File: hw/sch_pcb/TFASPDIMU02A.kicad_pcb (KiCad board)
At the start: 2 copper layers, 30 x 15 mm, 39 parts, among them J1 SM04B-GHS-TB, M1 HOLE_TF, M2 HOLE_TF, M3 HOLE_TF, M4 HOLE_TF, M7 HOLE_TF, M8 HOLE_TF, U1 SDP3x, U2 ICM-20948, U3 TCA9617A, U4 MIC5504-3.3YM5-TR, U5 MIC5504-1.8YM5-TR, U6 TCA9617A

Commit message: Edit PCB
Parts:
- added JP2: SolderJumper_3_Bridged12, Jumper:SolderJumper-3_P1.3mm_Bridged12_RoundedPad1.0x1.5mm, F.Cu at (4.32, -3.05)
- JP1: moved to F.Cu
- moved JP1 8.76 mm to (17.3, -12.2), turned to 90 degrees
- moved R3 4.35 mm to (18.0, -10.0), turned to 0 degrees
- moved C8 3.91 mm to (16.3, -13.1), turned to -90 degrees
- moved M4 2.97 mm to (22.0, 2.92)
- moved U5 1.77 mm to (18.9, -12.8)
- moved C6 1.47 mm to (22.9, -12.6), turned to 0 degrees
- moved C4 1.47 mm to (14.6, -12.4)
- moved C9 1.45 mm to (15.7, -5.59), turned to -90 degrees
- moved R11 1.33 mm to (21.1, -10.0), turned to 180 degrees
- moved C5 1.03 mm to (25.5, -1.65), turned to 0 degrees
- moved U2 1.02 mm to (13.2, -9.53)
- moved C2 0.80 mm to (11.8, -12.3), turned to 180 degrees
- moved C12 0.76 mm to (18.5, -4.57), turned to 90 degrees
- moved D2 0.74 mm to (25.5, -13.2)
- moved C11 0.62 mm to (22.9, -11.2), turned to 0 degrees
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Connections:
- R10 pad 1: Net-(U1-Pad9) -> Net-(R10-Pad1)
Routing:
- net +1V8: track 0.00 -> 40.7 mm, vias 0 -> 2
- net +3V3: track 5.36 -> 42.7 mm, vias 0 -> 5
- net +5V: track 0.00 -> 32.8 mm
- net /P_SCL_1V8: track 0.00 -> 12.7 mm, vias 0 -> 2
- net /SCL_3V3: track 0.00 -> 11.9 mm, vias 0 -> 2
- net /P_SDA_1V8: track 0.00 -> 8.94 mm, vias 0 -> 2
- net /SDA_3V3: track 0.00 -> 8.74 mm, vias 0 -> 2
- net /SCL_1V8: track 0.00 -> 8.69 mm, vias 0 -> 2
- net /SDA_1V8: track 0.00 -> 8.11 mm, vias 0 -> 2
- net Net-(U1-Pad9): track 0.73 -> 7.92 mm, vias 0 -> 1
- net Net-(JP1-Pad2): track 0.00 -> 5.67 mm, vias 0 -> 1
- net GND: track 0.00 -> 4.65 mm, vias 0 -> 46
- net Net-(R1-Pad1): track 0.00 -> 4.65 mm
- net Net-(R11-Pad1): track 0.00 -> 3.40 mm
- net Net-(C4-Pad1): track 0.00 -> 1.72 mm
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
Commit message: Dimensions and layout improvement.
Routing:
- net +1V8: track 40.7 -> 42.1 mm
- net Net-(R1-Pad1): track 4.65 -> 3.85 mm
- net GND: track 4.65 -> 5.20 mm, vias 46 -> 47

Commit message: Edit PCB
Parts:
- moved U1 0.10 mm to (5.40, -8.15)
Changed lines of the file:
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@@
-(kicad_pcb (version 20210722) (generator pcbnew)
+(kicad_pcb (version 20210228) (generator pcbnew)
   (general
     (thickness 1.6)
@@
       (effects (font (size 1 1) (thickness 0.15)))
     )
-    (fp_poly (pts
-        (xy -0.9 -0.3)
-        (xy -0.4 -0.3)
-        (xy -0.4 0.3)
-        (xy -0.9 0.3)
-      ) (layer "F.Cu") (width 0) (fill solid))
+    (fp_poly (pts (xy -0.9 -0.3)
+      (xy -0.4 -0.3)
+      (xy -0.4 0.3)
+      (xy -0.9 0.3)) (layer "F.Cu") (width 0) (fill solid))
     (fp_line (start 1.4 1) (end -1.4 1) (layer "F.SilkS") (width 0.12))
     (fp_line (start -1.2 1.2) (end -1.5 1.5) (layer "F.SilkS") (width 0.12))
@@
         (gr_circle (center 0 -0.25) (end 0.5 -0.25) (width 0) (fill yes))
         (gr_poly (pts
-            (xy 0.55 0.75)
-            (xy 0 0.75)
-            (xy 0 -0.75)
-            (xy 0.55 -0.75)
-          ) (width 0) (fill yes))
+          (xy 0.55 0.75)
+          (xy 0 0.75)
+          (xy 0 -0.75)
+          (xy 0.55 -0.75)
+        ) (width 0) (fill yes))
       ))
     (pad "2" smd rect locked (at 0 0 180) (size 1 1.5) (layers "F.Cu" "F.Mask")
@@
         (gr_circle (center 0 -0.25) (end 0.5 -0.25) (width 0) (fill yes))
         (gr_poly (pts
-            (xy 0 0.75)
-            (xy -0.55 0.75)
-            (xy -0.55 -0.75)
-            (xy 0 -0.75)
-          ) (width 0) (fill yes))
+          (xy 0 0.75)
+          (xy -0.55 0.75)
+          (xy -0.55 -0.75)
+          (xy 0 -0.75)
+        ) (width 0) (fill yes))
       ))
   )
@@
       (effects (font (size 1 1) (thickness 0.15)))
     )
-    (fp_poly (pts
-        (xy -0.9 -0.3)
-        (xy -0.4 -0.3)
-        (xy -0.4 0.3)
-        (xy -0.9 0.3)
-      ) (layer "F.Cu") (width 0) (fill solid))
+    (fp_poly (pts (xy -0.9 -0.3)
+      (xy -0.4 -0.3)
+      (xy -0.4 0.3)
+      (xy -0.9 0.3)) (layer "F.Cu") (width 0) (fill solid))
     (fp_line (start -2.05 0.3) (end -2.05 -0.3) (layer "F.SilkS") (width 0.12))
     (fp_line (start -1.2 1.2) (end -0.9 1.5) (layer "F.SilkS") (width 0.12))
@@
         (gr_circle (center 0 -0.25) (end 0.5 -0.25) (width 0) (fill yes))
         (gr_poly (pts
-            (xy 0.55 0.75)
-            (xy 0 0.75)
-            (xy 0 -0.75)
-            (xy 0.55 -0.75)
-          ) (width 0) (fill yes))
+          (xy 0.55 0.75)
+          (xy 0 0.75)
+          (xy 0 -0.75)
+          (xy 0.55 -0.75)
+        ) (width 0) (fill yes))
       ))
     (pad "2" smd rect locked (at 0 0 90) (size 1 1.5) (layers "F.Cu" "F.Mask")
@@
         (gr_circle (center 0 -0.25) (end 0.5 -0.25) (width 0) (fill yes))
         (gr_poly (pts
-            (xy 0 0.75)
-            (xy -0.55 0.75)
-            (xy -0.55 -0.75)
-            (xy 0 -0.75)
-          ) (width 0) (fill yes))
+          (xy 0 0.75)
+          (xy -0.55 0.75)
+          (xy -0.55 -0.75)
+          (xy 0 -0.75)
+        ) (width 0) (fill yes))
       ))
   )
@@
   )
   (footprint "Mlab_IO:SDP3x" locked (layer "B.Cu")
-    (at 5.4 -8.25 180)
+    (at 5.4 -8.15 180)
     (property "Sheetfile" "TFASPDIMU02A.kicad_sch")
     (property "Sheetname" "")
@@
   (segment (start 5.888 -2.288) (end 5.334 -2.288) (width 0.3) (layer "B.Cu") (net 3))
   (segment (start 8.6085 -4.531) (end 8.509 -4.6305) (width 0.3) (layer "B.Cu") (net 3))
-  (segment (start 9.915 -5.442) (end 10.569 -6.096) (width 0.3) (layer "B.Cu") (net 3))
   (segment (start 21.717 -5.209) (end 22.957 -5.209) (width 0.4) (layer "B.Cu") (net 3))
   (segment (start 21.717 -5.209) (end 21.032081 -5.209) (width 0.4) (layer "B.Cu") (net 3))
@@
   (segment (start 5.334 -2.288) (end 5.212 -2.288) (width 0.3) (layer "B.Cu") (net 3))
   (segment (start 4.473 -3.429) (end 4.473 -3.027) (width 0.3) (layer "B.Cu") (net 3))
+  (segment (start 9.915 -4.531) (end 10.119 -4.531) (width 0.3) (layer "B.Cu") (net 3))
   (segment (start 15.51 -10.525) (end 16.129 -9.906) (width 0.2) (layer "B.Cu") (net 3))
+  (segment (start 10.119 -4.531) (end 10.569 -4.981) (width 0.3) (layer "B.Cu") (net 3))
   (segment (start 6.731 -2.536) (end 6.136 -2.536) (width 0.3) (layer "B.Cu") (net 3))
   (segment (start 21.032081 -5.209) (end 20.88797 -5.064889) (width 0.4) (layer "B.Cu") (net 3))
   (segment (start 22.851 -6.518) (end 22.851 -5.315) (width 0.3) (layer "B.Cu") (net 3))
   (segment (start 22.957 -5.209) (end 22.987 -5.179) (width 0.4) (layer "B.Cu") (net 3))
+  (segment (start 10.569 -4.981) (end 10.569 -6.096) (width 0.3) (layer "B.Cu") (net 3))
   (segment (start 6.136 -2.536) (end 5.888 -2.288) (width 0.3) (layer "B.Cu") (net 3))
   (segment (start 18.542 -2.766) (end 19.022 -2.766) (width 0.4) (layer "B.Cu") (net 3))
   (segment (start 16.129 -9.906) (end 17.397 -9.906) (width 0.2) (layer "B.Cu") (net 3))
-  (segment (start 9.915 -4.531) (end 9.915 -5.442) (width 0.3) (layer "B.Cu") (net 3))
   (segment (start 16.76409 -9.906) (end 16.868069 -9.802021) (width 0.2) (layer "B.Cu") (net 3))
   (segment (start 4.4 -5.55) (end 4.4 -3.502) (width 0.3) (layer "B.Cu") (net 3))
@@
       )
     )
+  )
+  (zone (net 0) (net_name "") (layers F&B.Cu) (hatch edge 0.508)
+    (connect_pads (clearance 0))
+    (min_thickness 0.254)
+    (keepout (tracks not_allowed) (vias not_allowed) (pads not_allowed ) (copperpour allowed) (footprints allowed))
+    (fill (thermal_gap 0.508) (thermal_bridge_width 0.508))
+    (polygon
+      (pts
+        (xy 14.224 -8.509)
+        (xy 12.192 -8.509)
+        (xy 12.192 -10.541)
+        (xy 14.224 -10.541)
+      )
+    )
+  )
+  (zone (net 0) (net_name "") (layers F&B.Cu) (hatch edge 0.508)
+    (connect_pads (clearance 0))
+    (min_thickness 0.254)
+    (keepout (tracks not_allowed) (vias not_allowed) (pads not_allowed ) (copperpour allowed) (footprints allowed))
+    (fill (thermal_gap 0.508) (thermal_bridge_width 0.508))
+    (polygon
+      (pts
+        (xy 14.224 -8.509)
+        (xy 12.192 -8.509)
+        (xy 12.192 -10.541)
+        (xy 14.224 -10.541)
+      )
+    )

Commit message: Edit PCB. #1
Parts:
- removed M4, M8: HOLE_TF, Mlab_Mechanical:dira_3mm
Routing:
- net Net-(JP2-Pad2): track 7.92 -> 6.59 mm

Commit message: Edit PCB
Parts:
- added G***: LOGO, MLAB_LOGA:TF 14x6,6, F.Cu at (8.38, -9.40)
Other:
- board text added: "TFASPDIMU02A"
- board text removed: "I2C 1 - 5V 2 - SCL 4 - SDA 7 - GND"

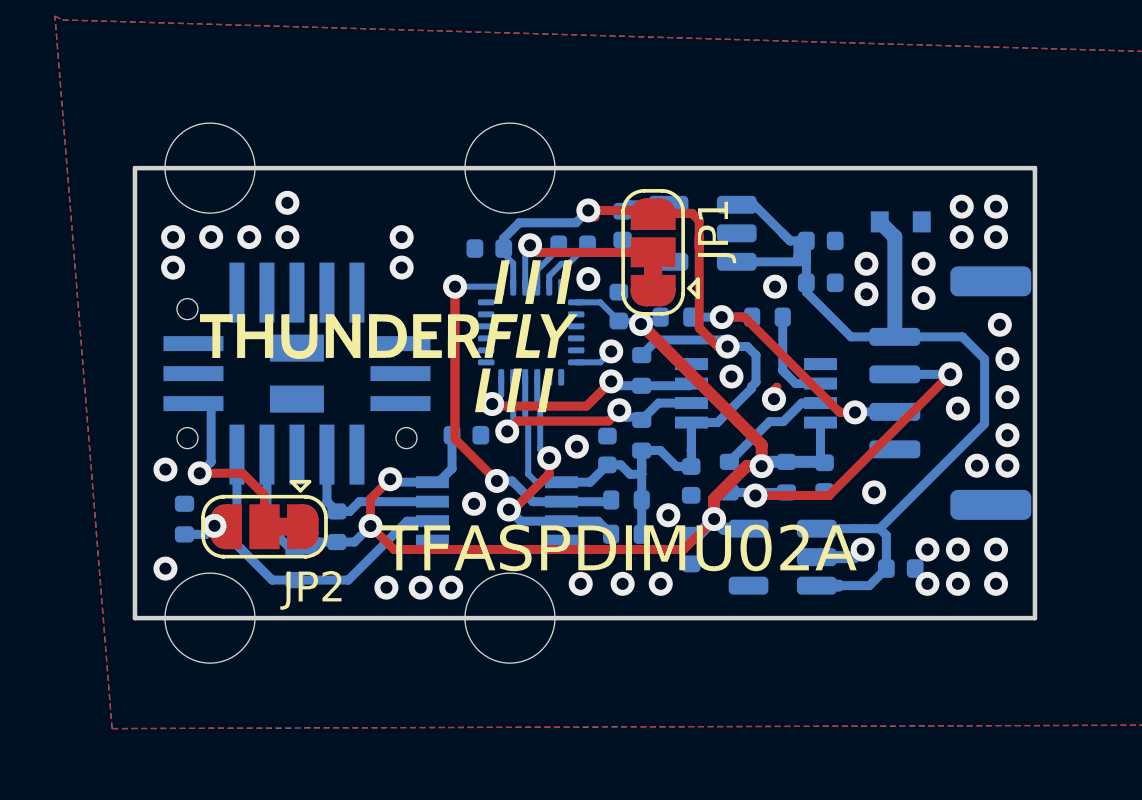
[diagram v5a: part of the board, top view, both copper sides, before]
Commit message: Layout and silkscreen improvements.
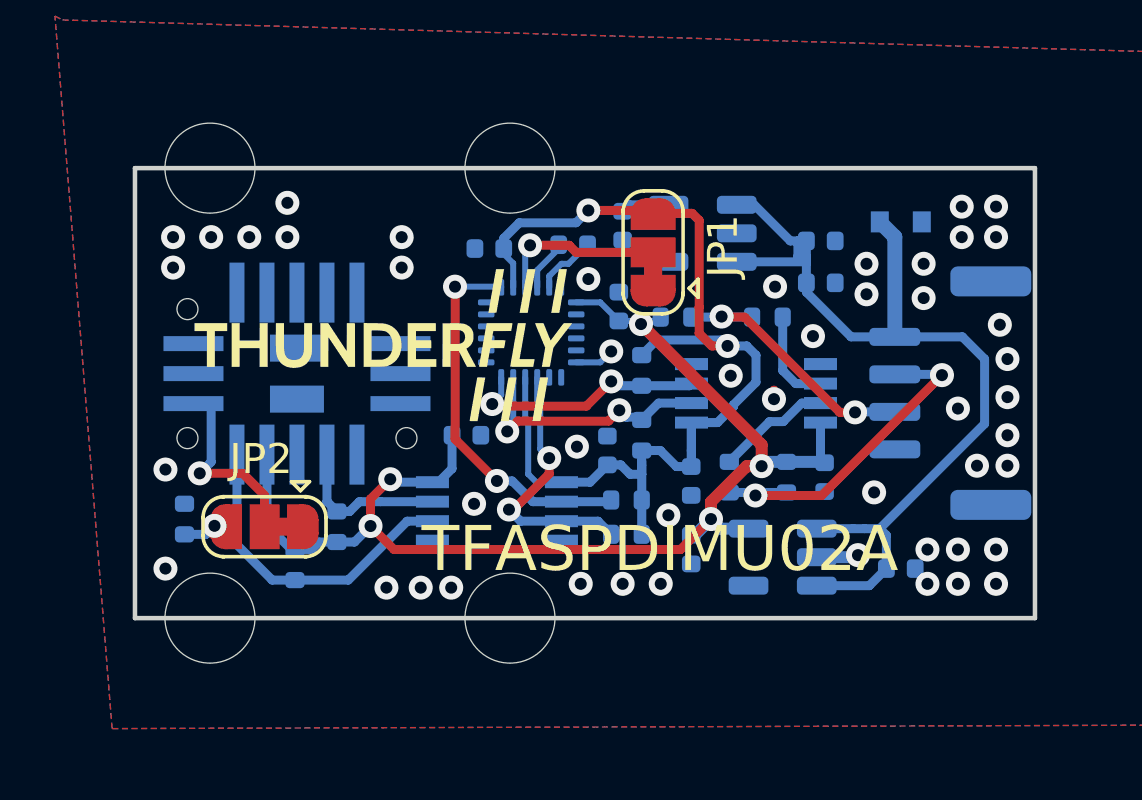
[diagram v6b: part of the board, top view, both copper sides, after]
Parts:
- moved G*** 0.35 mm to (8.20, -9.10)
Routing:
- net +1V8: track 42.1 -> 40.5 mm
- net +5V: track 32.8 -> 31.7 mm
- net /SCL_3V3: track 12.0 -> 11.5 mm
- net GND: track 5.20 -> 5.05 mm, vias 47 -> 48

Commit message: Edit PCB
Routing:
- net GND: vias 48 -> 47
